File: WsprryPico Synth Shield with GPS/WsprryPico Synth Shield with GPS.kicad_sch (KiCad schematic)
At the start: 48 parts, among them J11 1x20 socket, J12 1x20 socket, J61 SMA 50ohm, J71 U.FL 50ohm, Q61 BS170, SW11 Push, U21 TPS7A2033, U31 TPS22918, U51 Si5351A-B-GTR, U71 ATGM336H-5N31, Y41 25MHz TCXO

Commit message: Rename synth shield project to WsprryPico Synth Shield with GPS
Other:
- title: WsprryPico Synth Shield -> WsprryPico Synth Shield with GPS

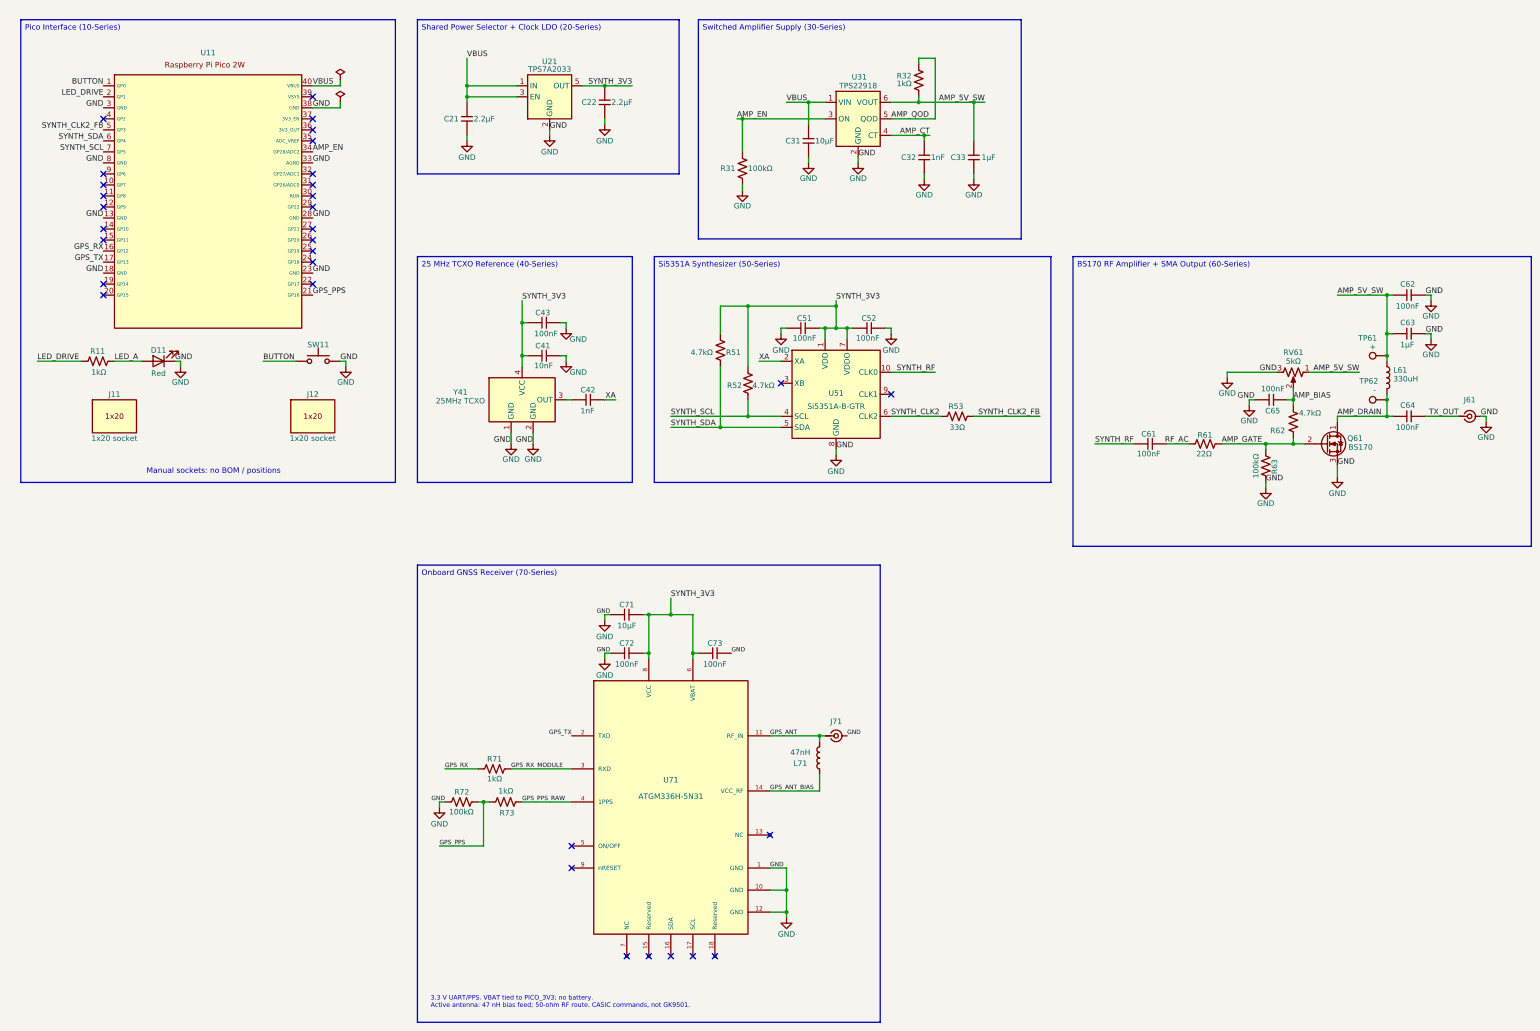
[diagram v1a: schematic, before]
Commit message: Add silkscreen and version
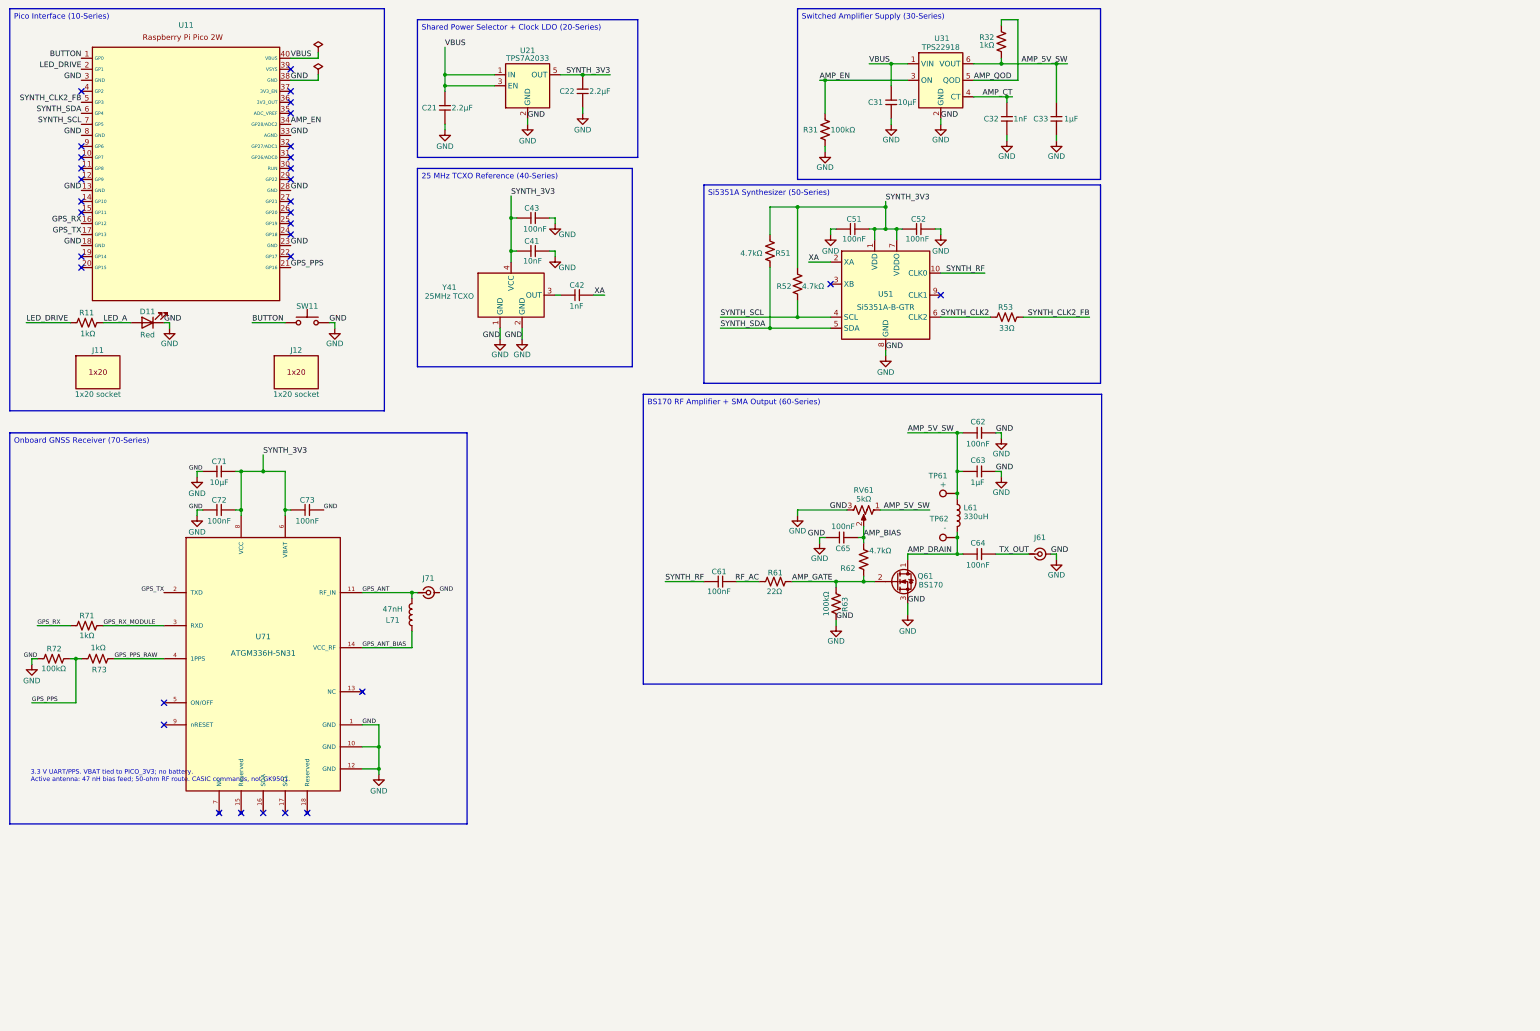
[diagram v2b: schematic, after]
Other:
- note removed: "Manual sockets: no BOM / positions"
- moved on the sheet: C21, C22, C31, C32, C33, C41, C42, C43, C51, C52, C61, C62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
